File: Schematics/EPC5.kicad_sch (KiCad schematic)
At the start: 35 parts, among them U13 ICE40HX4K-TQ144, U8 TLV62568DBV, U9 TLV62568DBV

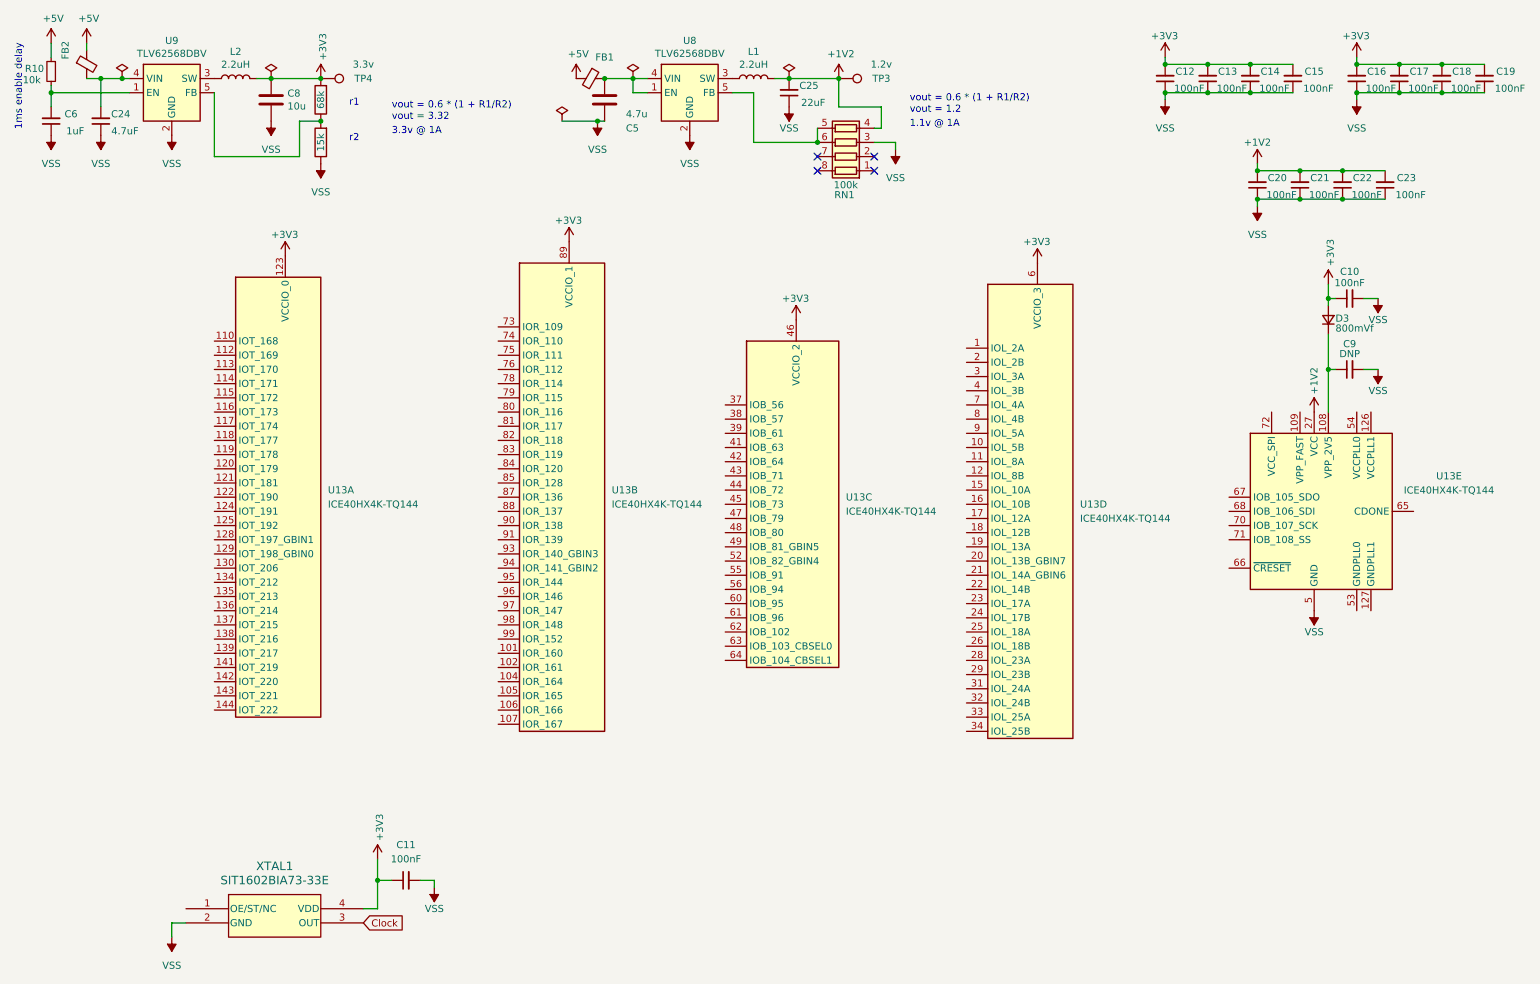
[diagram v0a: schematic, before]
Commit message: Need to order stencil
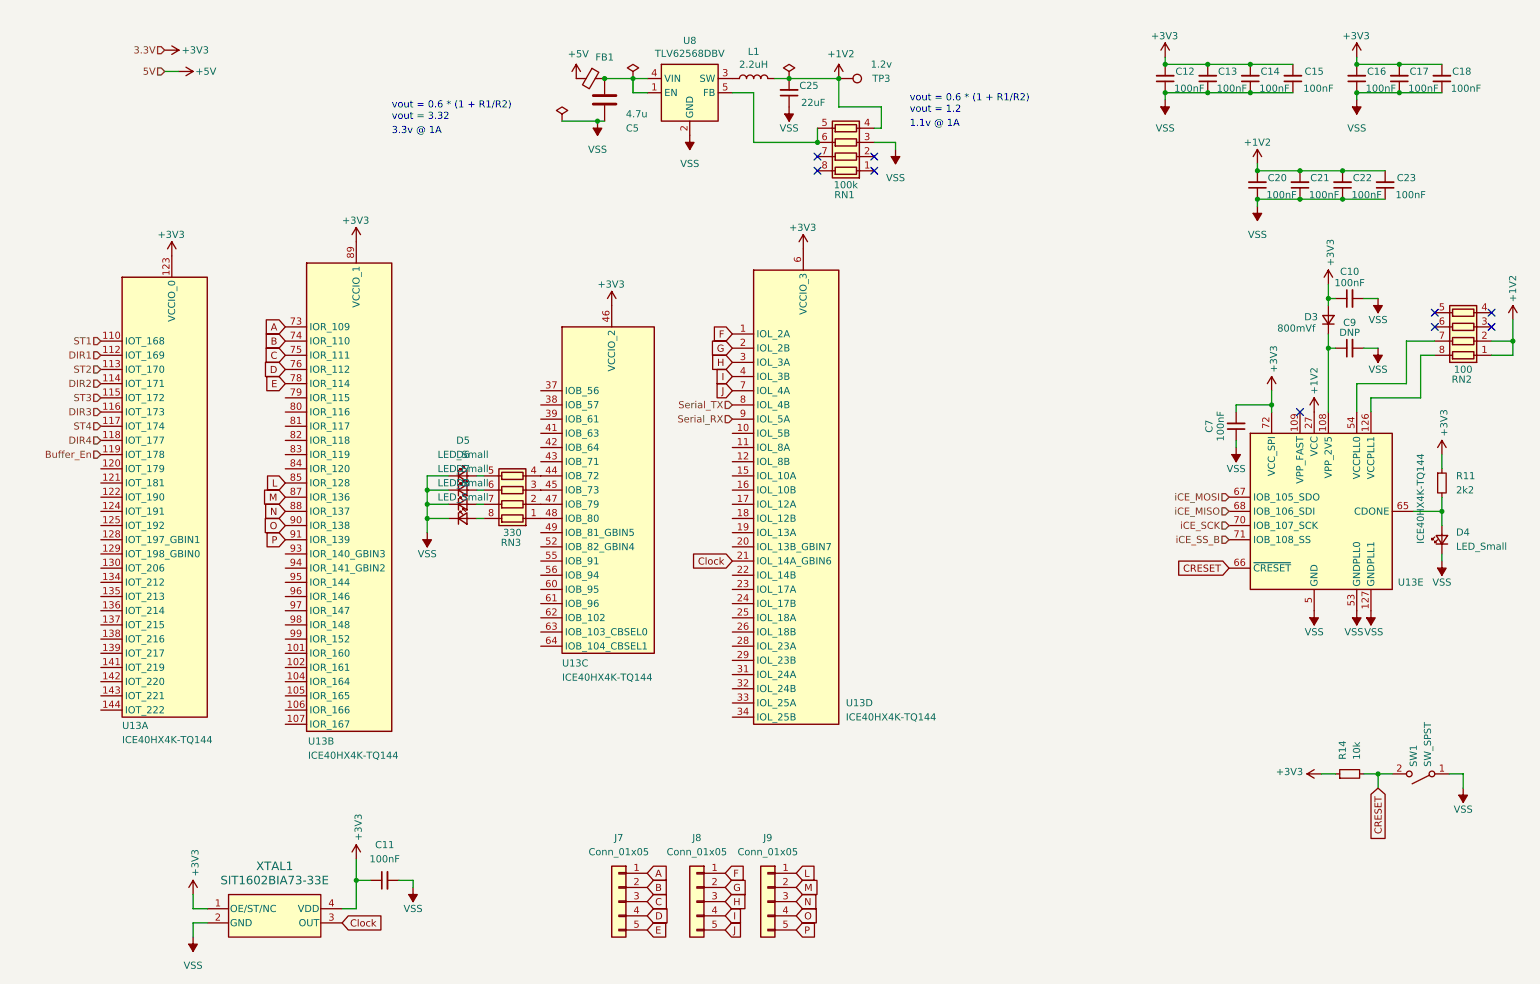
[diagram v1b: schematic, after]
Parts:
- removed C19: 100nF, symbol Device:C_Small
- removed C24: 4.7uF, symbol Device:C_Small
- removed C6: 1uF, symbol Device:C_Small
- removed C8: 10u, Capacitor_SMD:C_0805_2012Metric, symbol Device:C
- removed FB2: Ferrite_Bead_Small, Inductor_SMD:L_0805_2012Metric, symbol basic-ecp5-pcb-rescue:Ferrite_Bead_Small-Device
- removed L2: 2.2uH, Inductor_SMD:L_Taiyo-Yuden_NR-40xx, symbol Device:L
- removed R10: 10k, symbol Device:R_Small
- removed R12: 68k, Resistor_SMD:R_0805_2012Metric, symbol Device:R
- removed R13: 15k, Resistor_SMD:R_0805_2012Metric, symbol Device:R
- removed TP4: 3.3v, TestPoint:TestPoint_THTPad_D1.0mm_Drill0.5mm, symbol Connector:TestPoint
- removed U9: TLV62568DBV, Package_TO_SOT_SMD:SOT-23-5, symbol Regulator_Switching:TLV62568DBV
- added C7: 100nF, Capacitor_SMD:C_0805_2012Metric, symbol Device:C_Small
- added D4, D5, D6, D7, D8: LED_Small, LED_SMD:LED_0805_2012Metric, symbol Device:LED_Small
- added J7, J8, J9: Conn_01x05, Connector_PinHeader_2.54mm:PinHeader_1x05_P2.54mm_Vertical, symbol Connector_Generic:Conn_01x05
- added R11: 2k2, Resistor_SMD:R_0805_2012Metric, symbol Device:R_Small
- added R14: 10k, Resistor_SMD:R_0805_2012Metric, symbol Device:R_Small
- added RN2: 100, Resistor_SMD:R_Array_Convex_4x0603, symbol Device:R_Pack04
- added RN3: 330, Resistor_SMD:R_Array_Convex_4x0603, symbol Device:R_Pack04
- added SW1: SW_SPST, UE_Buttons:TS3315A, symbol Switch:SW_SPST
- C10, C11, C12, C13, C14, C15, C16, C17, C18, C20, C21, C22, C23, C25, C9: footprint (none) -> Capacitor_SMD:C_0805_2012Metric
- D3: footprint (none) -> Diode_SMD:D_0805_2012Metric
- RN1: footprint (none) -> Resistor_SMD:R_Array_Convex_4x0603
- XTAL1: footprint SON4_SIT1602-7_SIT -> UE_Misc:SON4_SIT1602-7_SIT
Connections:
- net +1V2: now also RN2.1 (R1.1), RN2.2 (R2.1)
- net +3V3: now also U13.72 (VCC_SPI), XTAL1.1 (OE/ST/NC), C7.2, R11.1, R14.1
- net Clock: now also U13.21 (IOL_14A_GBIN6)
- net VSS: now also U13.127 (GNDPLL1), U13.53 (GNDPLL0), C7.1, D4.1 (K), D5.1 (K), D6.1 (K), D7.1 (K), D8.1 (K), SW1.1 (A)
- net at U13.126 (VCCPLL1): now also RN2.8 (R1.2)
- net at U13.54 (VCCPLL0): now also RN2.7 (R2.2)
- net at U13.65 (CDONE): now also D4.2 (A), R11.2
- net CRESET: now reaches U13.66 (~{CRESET})
- net CRESET: now also R14.2, SW1.2 (B)
- net iCE_MOSI: now reaches U13.67 (IOB_105_SDO)
- net iCE_MISO: now reaches U13.68 (IOB_106_SDI)
- net iCE_SCK: now reaches U13.70 (IOB_107_SCK)
- net iCE_SS_B: now reaches U13.71 (IOB_108_SS)
- net F: now reaches U13.1 (IOL_2A)
- net F: now also J8.1 (Pin_1)
- net G: now reaches U13.2 (IOL_2B)
- net G: now also J8.2 (Pin_2)
- net H: now reaches U13.3 (IOL_3A)
- net H: now also J8.3 (Pin_3)
- net I: now reaches U13.4 (IOL_3B)
- net I: now also J8.4 (Pin_4)
- net J: now reaches U13.7 (IOL_4A)
- net J: now also J8.5 (Pin_5)
- net Serial_TX: now reaches U13.8 (IOL_4B)
- net Serial_RX: now reaches U13.9 (IOL_5A)
- net A: now reaches U13.73 (IOR_109)
- net A: now also J7.1 (Pin_1)
- net B: now reaches U13.74 (IOR_110)
- net B: now also J7.2 (Pin_2)
- net C: now reaches U13.75 (IOR_111)
- net C: now also J7.3 (Pin_3)
- net D: now reaches U13.76 (IOR_112)
- net D: now also J7.4 (Pin_4)
- net E: now reaches U13.78 (IOR_114)
- net E: now also J7.5 (Pin_5)
- net L: now reaches U13.85 (IOR_128)
- net L: now also J9.1 (Pin_1)
- net M: now reaches U13.87 (IOR_136)
- net M: now also J9.2 (Pin_2)
- net N: now reaches U13.88 (IOR_137)
- net N: now also J9.3 (Pin_3)
- net O: now reaches U13.90 (IOR_138)
- net O: now also J9.4 (Pin_4)
- net P: now reaches U13.91 (IOR_139)
- net P: now also J9.5 (Pin_5)
- net at U13.44 (IOB_72): now also RN3.4 (R4.1)
- net at U13.45 (IOB_73): now also RN3.3 (R3.1)
- net at U13.47 (IOB_79): now also RN3.2 (R2.1)
- net at U13.48 (IOB_80): now also RN3.1 (R1.1)
- net ST1: now reaches U13.110 (IOT_168)
- net DIR1: now reaches U13.112 (IOT_169)
- net ST2: now reaches U13.113 (IOT_170)
- net DIR2: now reaches U13.114 (IOT_171)
- net ST3: now reaches U13.115 (IOT_172)
- net DIR3: now reaches U13.116 (IOT_173)
- net ST4: now reaches U13.117 (IOT_174)
- net DIR4: now reaches U13.118 (IOT_177)
- net Buffer_En: now reaches U13.119 (IOT_178)
- new net: D7.2 (A), RN3.7 (R2.2)
- new net: D6.2 (A), RN3.6 (R3.2)
- new net: D5.2 (A), RN3.5 (R4.2)
- new net: D8.2 (A), RN3.8 (R1.2)
- no-connect marks 4 -> 9
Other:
- note removed: "1ms enable delay"
- note removed: "r1"
- note removed: "r2"
- moved on the sheet: C11, C9, U13A, U13B, U13C, U13D
